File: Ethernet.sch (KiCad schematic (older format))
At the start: 0 parts

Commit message: Updates common component library
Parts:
- added C? (x2): 30p, Capacitor_SMD:C_0805_2012Metric, symbol Device:C_Small
- added R? (x5): 10k, Resistor_SMD:R_0805_2012Metric, symbol Device:R_Small
- added R? (x5): 33, Resistor_SMD:R_0805_2012Metric, symbol Device:R_Small
- added R?: 1.5k, Resistor_SMD:R_0805_2012Metric, symbol Device:R_Small
- added U?: USBLC6-4SC6, Package_TO_SOT_SMD:SOT-23-6, symbol Power_Protection:USBLC6-4SC6
- added U?: LAN8742A-CZ-TR, UTSVT_ICs:LAN8742AI-CZ-TR, symbol utsvt-chips:LAN8742A-CZ-TR
- added Y?: 25M, Crystal:Crystal_SMD_HC49-SD, symbol Device:Crystal_Small
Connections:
- new net: R?.1, U?.10 (RXER/PHYAD0)
- new net: R?.1, R?.2, U?.11 (CRS_DV/MODE2)
- new net: R?.1, R?.1, U?.12 (MDIO)
- new net: R?.1, R?.1, U?.14 (nINT/REFCLK0)
- new net: C?.1, U?.4 (XTAL2), Y?.1
- new net: C?.1, U?.5 (XTAL1/CLKIN), Y?.2
- new net: R?.1, R?.2, U?.7 (RXD1/MODE1)
- new net: R?.1, R?.2, U?.8 (RXD0/MODE0)
- new net +3V3: R?.1, R?.1, R?.1, R?.2, R?.2
- new net GND: C?.2, C?.2, R?.2
- new net NRST: U?.15 (nRST)
- new net RMII_CRS_DV: R?.2
- new net RMII_MDC: U?.13 (MDC)
- new net RMII_MDIO: R?.2
- new net RMII_REF_CLK: R?.2
- new net RMII_RXD0: R?.2
- new net RMII_RXD1: R?.2
- new net RMII_TXD0: U?.17 (TXD0)
- new net RMII_TXD1: U?.18 (TXD1)
- new net RMII_TX_EN: U?.16 (TXEN)
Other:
- note added: "Following pinouts are referenced\noff of NUCLEO-F429ZI board"
- note added: "PA1"
- note added: "PA2"
- note added: "PA7"
- note added: "PB13"
- note added: "PC1"
- note added: "PC4"
- note added: "PC5"
- note added: "PG11"
- note added: "PG13"

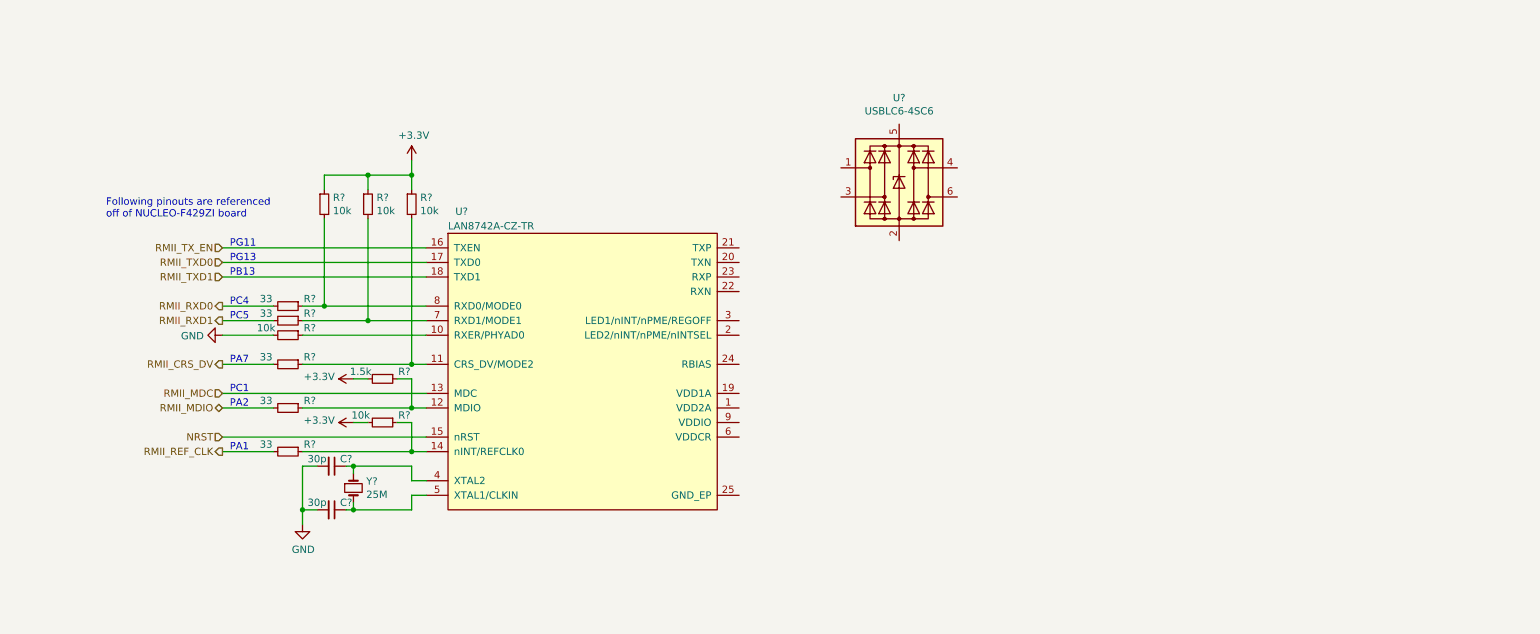
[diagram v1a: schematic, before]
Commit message: Adds ethernet schematics
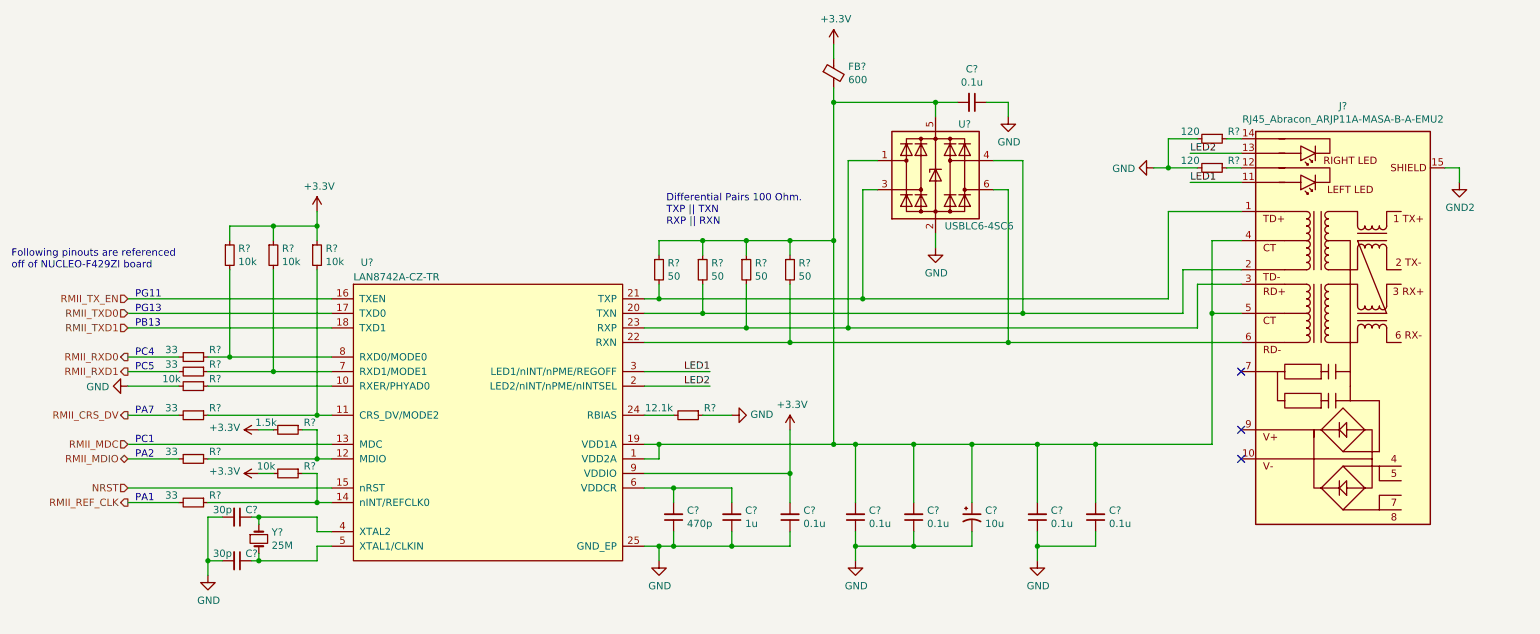
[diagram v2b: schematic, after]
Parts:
- added C? (x6): 0.1u, Capacitor_SMD:C_0805_2012Metric, symbol Device:C_Small
- added C?: 470p, Capacitor_SMD:C_0805_2012Metric, symbol Device:C_Small
- added C?: 1u, Capacitor_SMD:C_0805_2012Metric, symbol Device:C_Small
- added C?: 10u, Capacitor_Tantalum_SMD:CP_EIA-3216-18_Kemet-A, symbol Device:CP1_Small
- added FB?: 600, Inductor_SMD:L_0805_2012Metric, symbol Device:Ferrite_Bead_Small
- added J?: RJ45_Abracon_ARJP11A-MASA-B-A-EMU2, Connector_RJ:RJ45_Abracon_ARJP11A-MA_Horizontal, symbol Connector:RJ45_Abracon_ARJP11A-MASA-B-A-EMU2
- added R? (x4): 50, Resistor_SMD:R_0805_2012Metric, symbol Device:R_Small
- added R?: 12.1k, Resistor_SMD:R_0805_2012Metric, symbol Device:R_Small
- added R? (x2): 120, Resistor_SMD:R_0805_2012Metric, symbol Device:R_Small
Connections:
- net +3V3: now also U?.9 (VDDIO), C?.2, FB?.1
- net GND: now also U?.2 (GND), U?.25 (GND_EP), C?.1, C?.1, C?.1, C?.1, C?.1, C?.1, C?.1, C?.1, C?.2, R?.1, R?.2, R?.2
- net at U?.1 (I/O1): now also U?.23 (RXP), J?.3 (RD+), R?.2
- net at U?.3 (I/O2): now also U?.21 (TXP), J?.1 (TD+), R?.2
- net at U?.4 (I/O3): now also U?.20 (TXN), J?.2 (TD-), R?.2
- net at U?.5 (VBUS): now also U?.1 (VDD2A), U?.19 (VDD1A), C?.1, C?.2, C?.2, C?.2, C?.2, C?.2, FB?.2, J?.4 (CT), J?.5 (CT), R?.1, R?.1, R?.1, R?.1
- net at U?.6 (I/O4): now also U?.22 (RXN), J?.6 (RD-), R?.2
- net LED2: now reaches U?.2 (LED2/nINT/nPME/nINTSEL)
- net LED2: now also J?.13 (RLED+)
- net at U?.24 (RBIAS): now also R?.2
- net LED1: now reaches U?.3 (LED1/nINT/nPME/REGOFF)
- net LED1: now also J?.11 (LLED+)
- net at U?.6 (VDDCR): now also C?.2, C?.2
- new net: J?.12 (LLED-), R?.1
- new net: J?.14 (RLED-), R?.1
- new net GND2: J?.15 (SHIELD)
- no-connect marks 0 -> 3
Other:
- note added: "Differential Pairs 100 Ohm.\nTXP || TXN\nRXP || RXN"
- moved on the sheet: C?, R?, U?, Y?

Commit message: Adds GPS module to common library
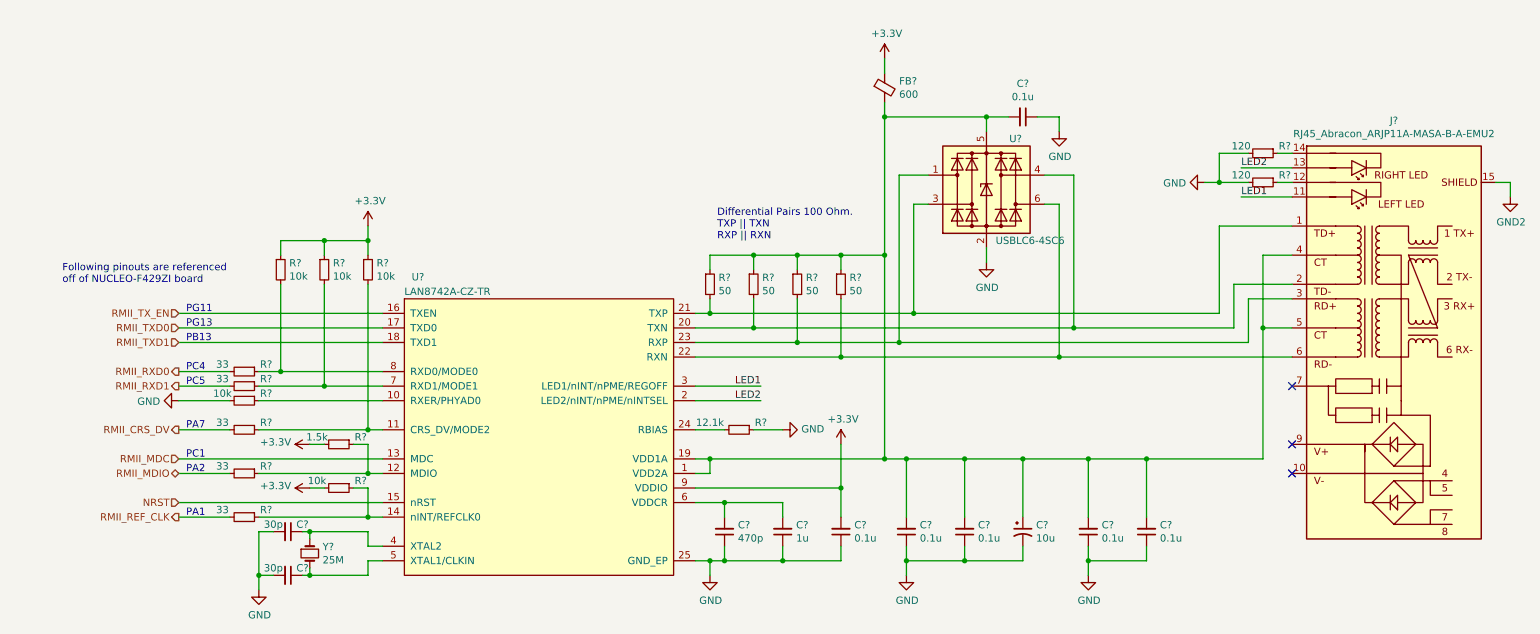
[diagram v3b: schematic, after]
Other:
- moved on the sheet: C?, FB?, J?, R?, U?, Y?

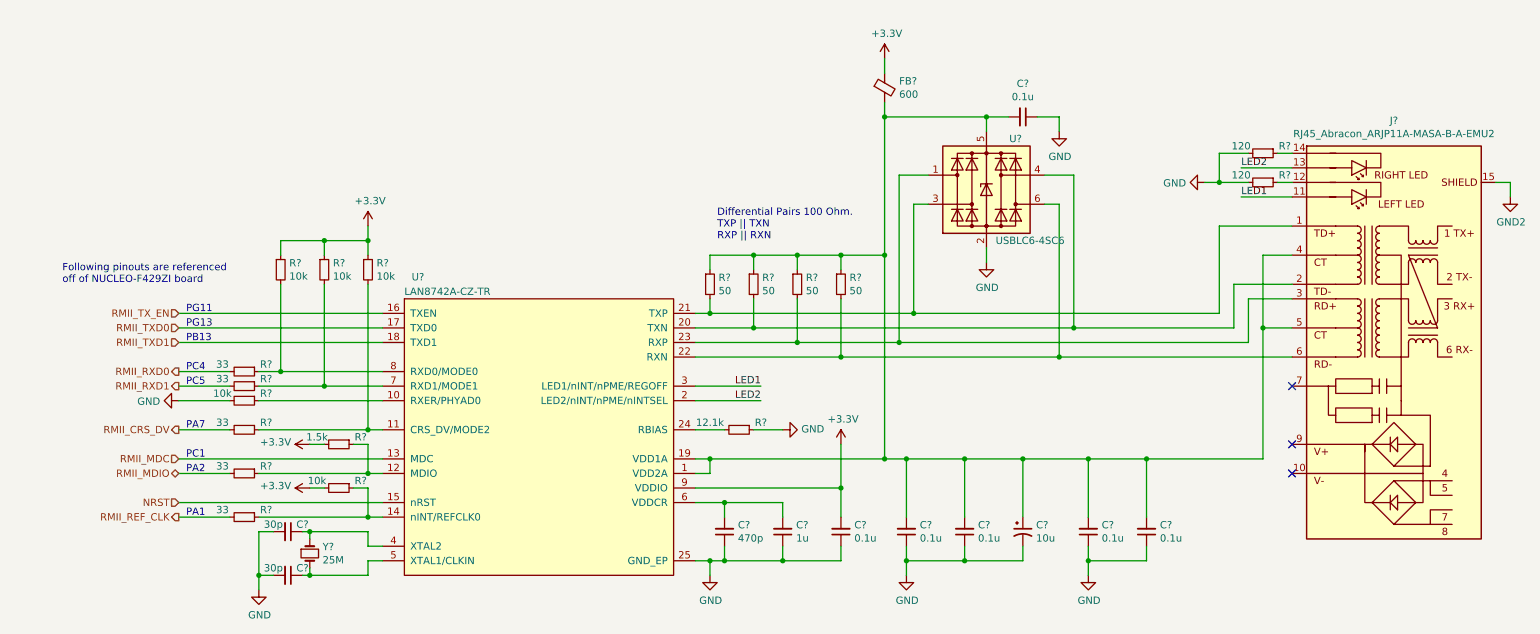
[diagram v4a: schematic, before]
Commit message: Initial layout of the Telemtry board.
The ethernet interface needs more work.
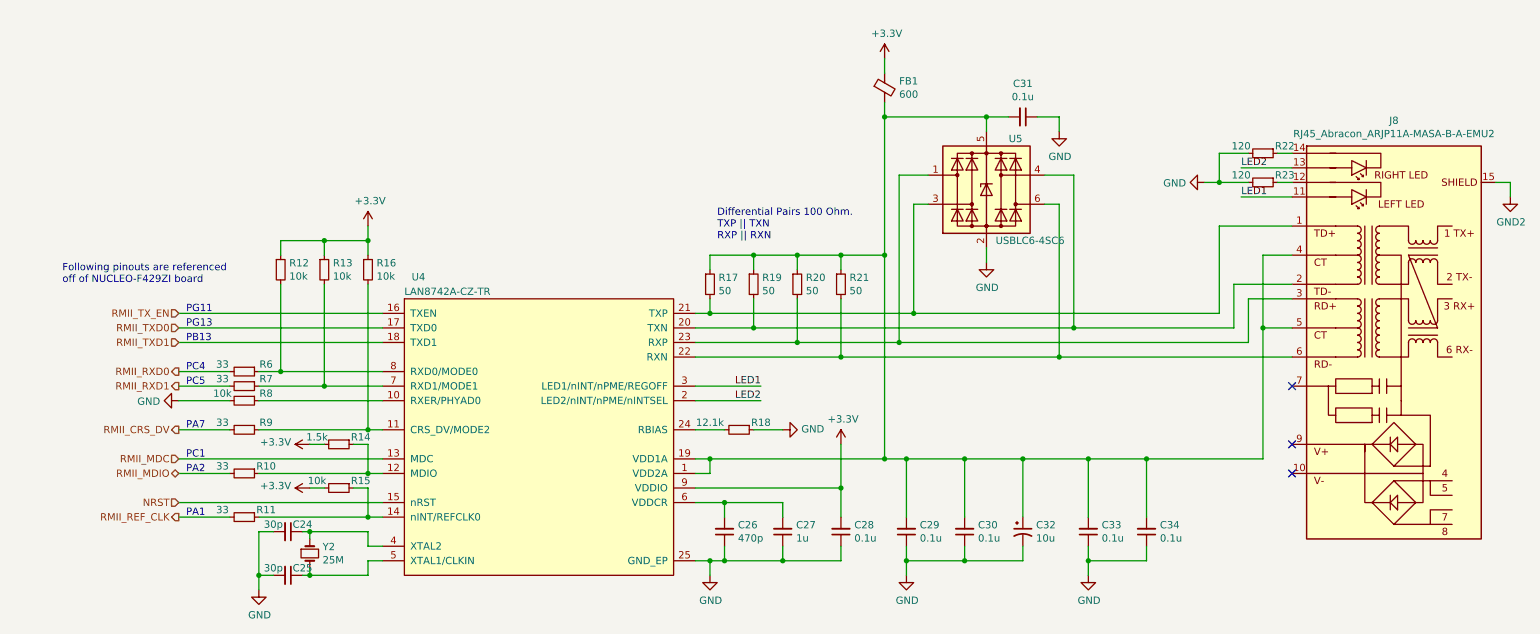
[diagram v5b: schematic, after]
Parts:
- gave numbers to parts that had none: 34

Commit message: Lay out the Telemetry board.
This is the initial draft of the Telemetry board layout. A few
debugging pins changed (on the SD card) for easier routing.

There is still some uncertainty with regard to the routing of the
Ethernet traces. According to my calculations, the differential
impedence between the RX+/- traces and the TX+/- traces is around
150R, which is 50% higher than one source was recommending. I am
uncertain how to reduce this though, and I am unclear as to how
much this will affect performance, especially when the traces
cover such a short distance.
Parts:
- J8: symbol Connector:RJ45_Abracon_ARJP11A-MASA-B-A-EMU2 -> Telemetry-Primary-rescue:RJ45_Abracon_ARJP11A-MASA-B-A-EMU2-Connector
- U5: symbol Power_Protection:USBLC6-4SC6 -> Telemetry-Primary-rescue:USBLC6-4SC6-Power_Protection
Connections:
- net RX+: now reaches J8.3 (RD+), R20.2, U4.23 (RXP), U5.1 (I/O1)
- net TX+: now reaches J8.1 (TD+), R17.2, U4.21 (TXP), U5.3 (I/O2)
- net TX-: now reaches J8.2 (TD-), R19.2, U4.20 (TXN), U5.4 (I/O3)
- net RX-: now reaches J8.6 (RD-), R21.2, U4.22 (RXN), U5.6 (I/O4)
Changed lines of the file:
@@
 $EndDescr
 $Comp
-L Power_Protection:USBLC6-4SC6 U5
+L Telemetry-Primary-rescue:USBLC6-4SC6-Power_Protection U5
 U 1 1 5F8F389F
 P 7100 2500
@@
 $EndComp
 $Comp
-L Connector:RJ45_Abracon_ARJP11A-MASA-B-A-EMU2 J8
+L Telemetry-Primary-rescue:RJ45_Abracon_ARJP11A-MASA-B-A-EMU2-Connector J8
 U 1 1 5FA4E03B
 P 9900 3550
@@
 	7800 4350 8200 4350
 $Comp
-L power:GND2 #PWR0145
+L Telemetry-Primary-rescue:GND2-power #PWR0145
 U 1 1 5FA6BA5E
 P 10700 2550
@@
 Wire Wire Line
 	9000 3450 9000 4350
+Text Label 6700 3350 0    50   ~ 0
+TX+
+Text Label 6700 3450 0    50   ~ 0
+TX-
+Text Label 6700 3550 0    50   ~ 0
+RX+
+Text Label 6700 3650 0    50   ~ 0
+RX-
 $EndSCHEMATC
